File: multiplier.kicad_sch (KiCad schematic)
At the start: 10 parts

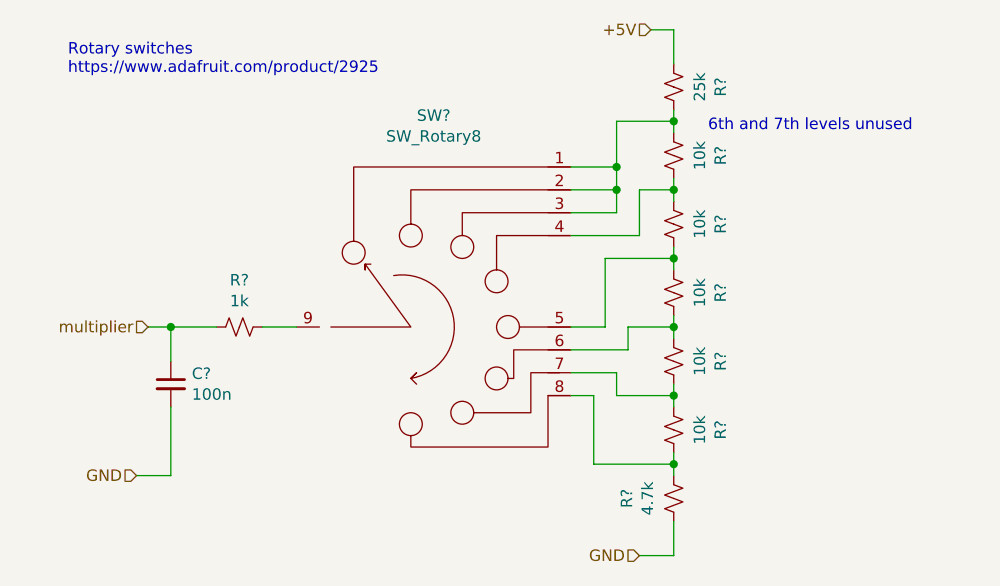
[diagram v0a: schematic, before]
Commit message: Separate IO from main board
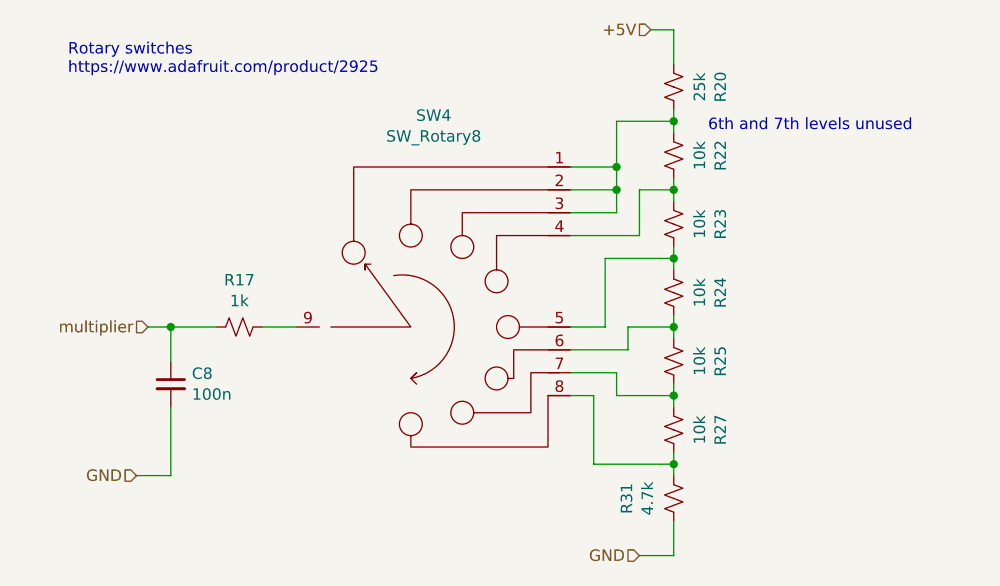
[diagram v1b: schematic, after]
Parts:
- gave numbers to parts that had none: 10
